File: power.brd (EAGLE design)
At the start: 90 x 77.5 mm, 34 parts, among them IC1 74HC125D, IC2 7805TV, IC3 7815TV

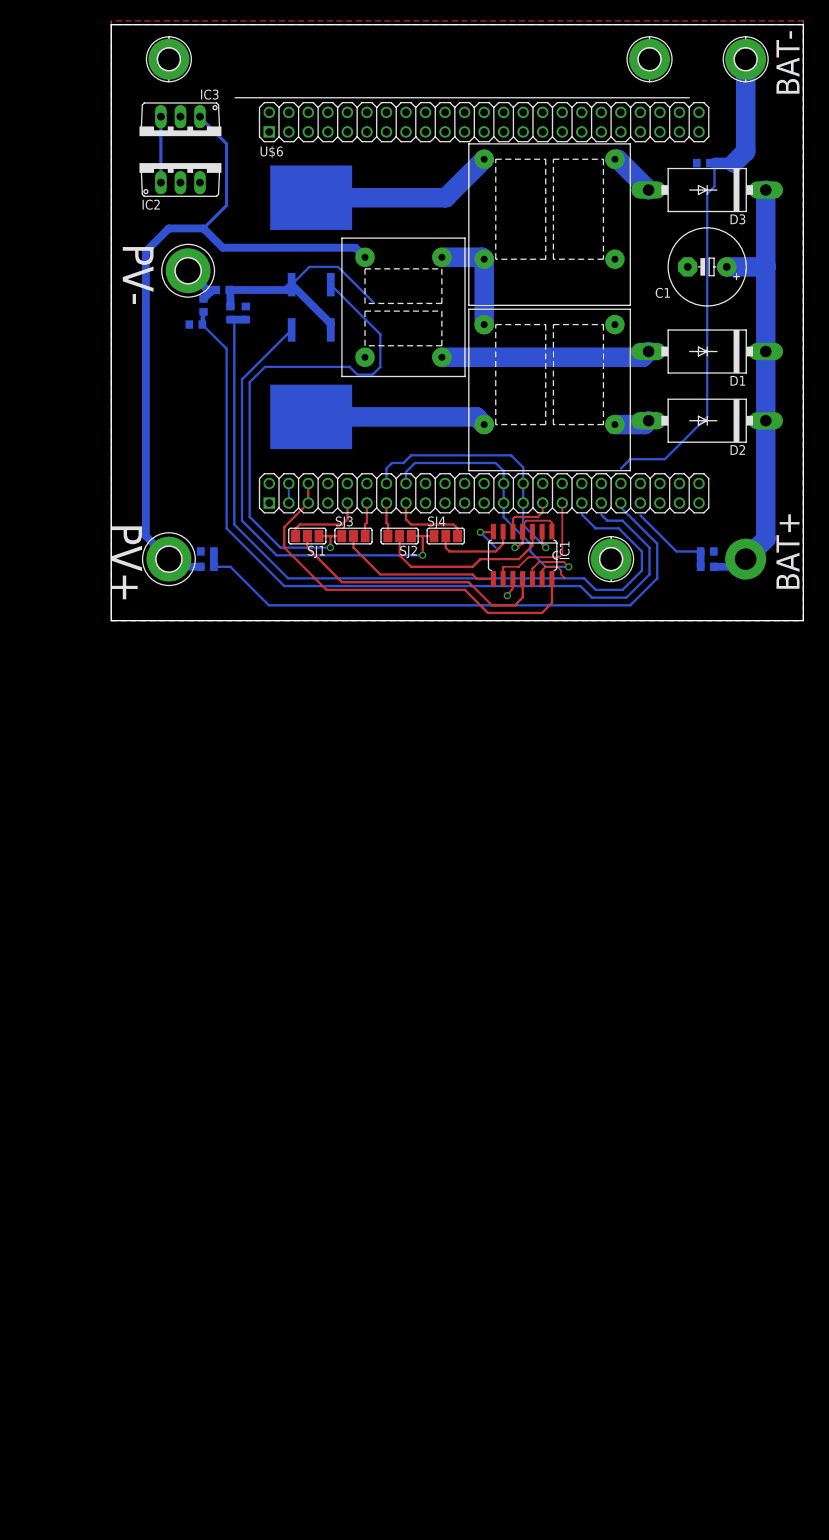
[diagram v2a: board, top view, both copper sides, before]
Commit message: added LTC4151 I2C IV monotors to the schematic and some other fixes.  The prototype doesn't work yet, so watch out.
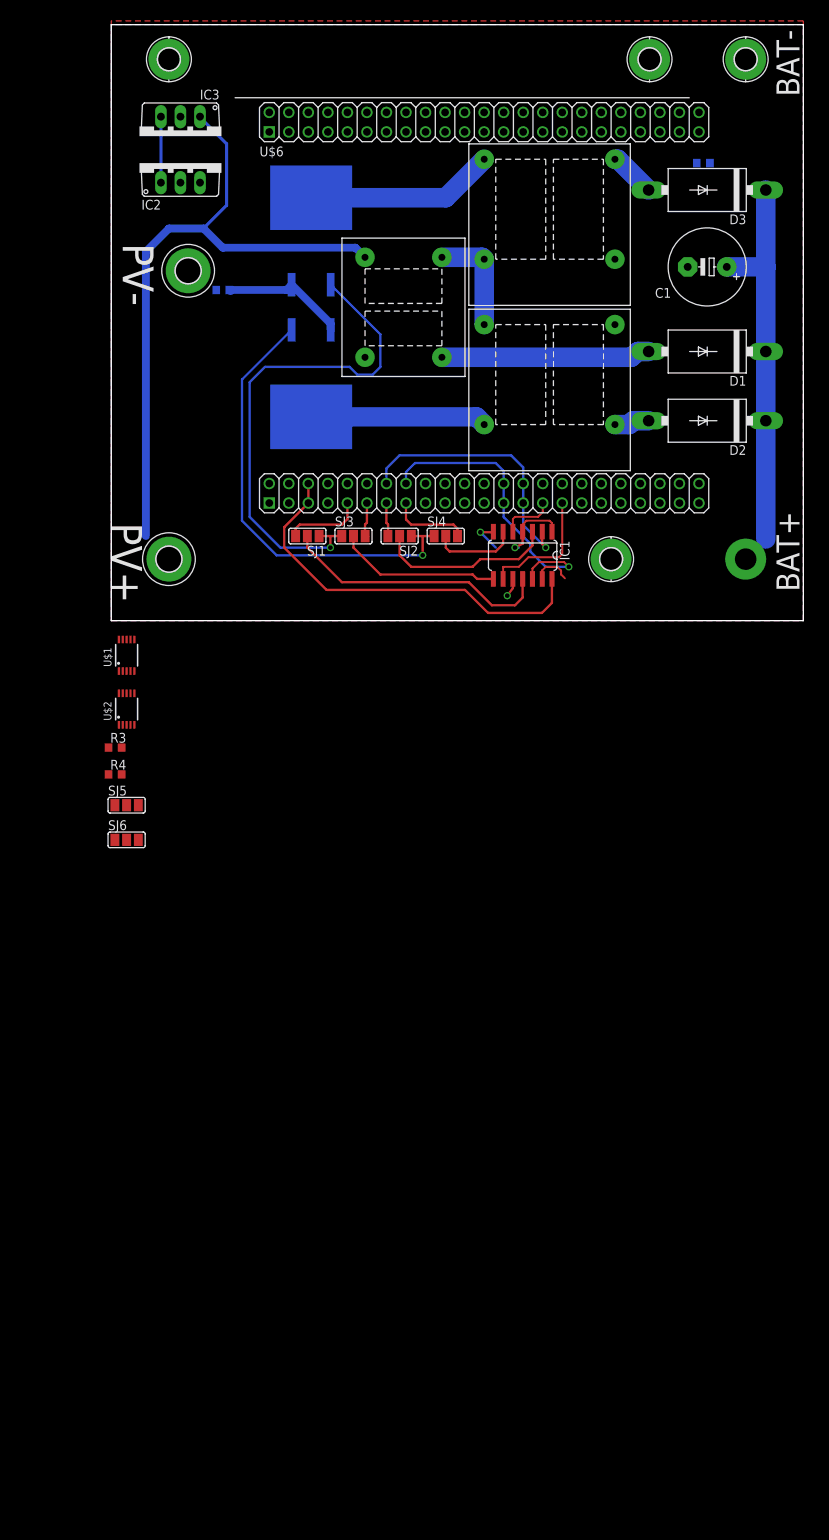
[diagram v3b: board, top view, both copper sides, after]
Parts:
- removed R10, R6, R8: 1k, rcl:R0603
- removed R5, R9: 51k, rcl:R0603
- removed R7: 15k, rcl:R0603
- added SJ5, SJ6: (no value), jumper:SJ_2
- added U$1, U$2: LTC4151, semiconductors:MSOP10
- R3: value 51k -> (none)
- R4: value 1k -> (none)
- moved R4 31.4 mm to (-2.00, -23.0), flipped to the top, turned to 0 degrees
- moved R3 26.4 mm to (-2.00, -19.5), flipped to the top, turned to 0 degrees
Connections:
- removed net N$17: R5.2, R6.2
- removed net N$18: R10.2, R9.2
- removed net VDD_3V3EXP: U$6.49, U$6.50
- new net +3V3: R3.2, R4.2, U$1.8, U$2.8, U$6.49, U$6.50
- new net N$14: R4.1, U$2.6, U$6.63
- new net N$26: SJ6.2, U$2.4
- net GND: now also BAT-.B2,8, SJ5.1, SJ6.1, U$1.9, U$2.3, U$2.9; no longer R1.1, R10.1, R4.1, R6.1, R8.1
- net N$10: now also SJ5.2, U$1.4; no longer R7.2, R8.2
- net N$12: now also C1.+, D1.C, D2.C, D3.C, R1.1, SJ6.3, U$2.1, U$2.2; no longer R3.2, R4.2
- net N$16: now also PV+.B3,3, SJ5.3, U$1.1, U$1.2, U$1.3; no longer PV-.B3,3, R5.1
- net N$4: now also BAT+.B2,8, IC3.1, U$2.10; no longer BAT-.B2,8
- net N$6: now also R2.2, U$1.10; no longer IC3.1, PV+.B3,3, R3.1
- net N$7: now also R3.1, U$2.7, U$6.64; no longer BAT+.B2,8, C1.+, D1.C, D2.C, D3.C, R7.1
- net N$8: now also PV-.B3,3; no longer R2.2, R9.1
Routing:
- net N$17: track 101.3 -> 0.00 mm
- net N$18: track 99.5 -> 0.00 mm
- net N$4: track 64.7 -> 0.00 mm
- net N$7: track 58.7 -> 0.00 mm
- net N$12: track 74.4 -> 50.5 mm
- net N$8: track 32.1 -> 16.4 mm
- net N$10: track 11.8 -> 0.00 mm
- net N$6: track 94.3 -> 85.4 mm
- net N$16: track 6.12 -> 1.41 mm
- net VDD_3V3EXP: track 2.54 -> 0.00 mm

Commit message: whomp
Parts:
- removed IC1: 74HC125D, 74xx-eu:SO14
- removed IC3: 7815TV, linear:TO220V
- removed SJ1, SJ2, SJ3, SJ4: (no value), jumper:SJ_2
- added R10, R11, R12, R13, R14, R15, R16, R17, R18, R19, R20, R21, R22, R23, R24, R25, R26, R27, R28, R29, R30, R7, R8, R9: 0, rcl:R0603
- added R5, R6: 10k, rcl:R0603
- U$7, U$8: value 45NO6LG -> SIA446DJ; device semiconductors:D2PAK-3 -> semiconductors:SC70-6L
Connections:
- removed net N$27: IC2.1, IC3.3
- new net N$17: R9.1, U$6.77
- new net N$18: R10.1, U$6.76
- new net N$30: R5.2, R6.1, U$1.5
- new net N$31: R26.1, U$6.43
- new net N$32: R27.1, U$6.42
- new net N$34: R29.1, U$6.40
- new net N$35: R30.1, U$6.39
- new net N$36: U$6.12
- new net N$39: R19.1, U$6.21
- new net N$40: R18.1, U$6.27
- new net N$41: R17.1, U$6.28
- new net N$42: R16.1, U$6.29
- new net N$43: U$6.30
- new net N$44: R10.2, R12.2, R14.2, R16.2, R18.2, R20.2, R22.2, R24.2, R26.2, R28.2, R30.2, R8.2, U$7.3
- new net N$45: R11.2, R13.2, R15.2, R17.2, R19.2, R21.2, R23.2, R25.2, R27.2, R29.2, R7.2, R9.2, U$8.3
- net GND: now also R6.2; no longer IC1.1, IC1.10, IC1.13, IC1.4, IC1.7, IC3.2
- net N$11: now also R15.1; no longer SJ1.1, SJ3.1, U$8.1
- net N$13: now also R21.1; no longer SJ2.1, SJ4.1, U$7.1
- net N$14: now also U$1.6, U$6.70; no longer U$6.63
- net N$19: now also R11.1, U$6.75; no longer SJ1.3, U$6.55
- net N$2: now also U$8.1, U$8.2, U$8.5, U$8.6; no longer U$8.4
- net N$20: now also R7.1, U$6.87; no longer IC1.3, SJ2.2
- net N$21: now also R8.1, U$6.88; no longer SJ3.3, U$6.57
- net N$22: now also R12.1, U$6.74; no longer SJ4.3, U$6.61
- net N$23: now also R13.1; no longer IC1.2, U$6.60, U$6.74
- net N$24: now also R14.1, U$6.71; no longer IC1.6, SJ4.2
- net N$25: now also R23.1, U$6.46; no longer IC1.11, SJ1.2
- net N$28: now also R24.1, U$6.45; no longer IC1.12, U$6.62, U$6.71, U$6.72
- net N$29: now also R25.1, U$6.44; no longer IC1.8, SJ3.2
- net N$3: now also U$7.1, U$7.2, U$7.5, U$7.6; no longer U$7.4
- net N$33: now also R28.1, U$6.41; no longer SJ2.3, U$6.59
- net N$37: now also R22.1, U$6.11; no longer IC1.5, U$6.75
- net N$38: now also R20.1, U$6.20; no longer IC1.9, U$6.77
- net N$4: now also IC2.1; no longer IC3.1
- net N$7: now also U$1.7, U$6.72; no longer U$6.64
- net N$8: now also R5.1, U$7.4, U$7.7, U$8.4, U$8.7; no longer U$7.3, U$8.3
- net VCC: no longer IC1.14
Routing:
- net N$11: track 66.1 -> 0.00 mm, vias 1 -> 0
- net N$13: track 58.3 -> 0.00 mm, vias 1 -> 0
- net N$28: track 39.5 -> 0.00 mm, vias 1 -> 0
- net N$25: track 35.4 -> 0.00 mm
- net N$23: track 35.0 -> 0.00 mm, vias 1 -> 0
- net N$8: track 16.4 -> 51.4 mm
- net N$20: track 23.3 -> 0.00 mm
- net GND: track 21.5 -> 0.00 mm, vias 3 -> 0
- net N$29: track 21.4 -> 0.00 mm
- net N$38: track 16.6 -> 0.00 mm
- net N$24: track 11.2 -> 0.00 mm
- net N$19: track 10.3 -> 0.00 mm
- net N$22: track 10.3 -> 0.00 mm
- net N$27: track 8.58 -> 0.00 mm
- net N$37: track 7.09 -> 0.00 mm
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
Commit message: don't worry, it's not as bad as it looks
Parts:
- R3, R4: value (none) -> 47k
- moved R29 198.5 mm to (67.3, 66.0), flipped to the bottom
- moved R30 196.0 mm to (64.8, 66.0), flipped to the bottom, turned to 90 degrees
- moved R27 195.2 mm to (71.1, 66.0), flipped to the bottom, turned to 90 degrees
- moved R28 193.0 mm to (69.8, 66.0), flipped to the bottom, turned to 90 degrees
- moved R25 191.1 mm to (72.4, 66.0), flipped to the bottom, turned to 90 degrees
- moved R26 189.7 mm to (73.7, 66.0), flipped to the bottom, turned to 90 degrees
- moved R23 187.5 mm to (74.9, 66.0), flipped to the bottom, turned to 90 degrees
- moved R24 186.0 mm to (76.2, 66.0), flipped to the bottom, turned to 90 degrees
- moved R21 169.4 mm to (31.8, 66.0), flipped to the bottom, turned to 90 degrees
- moved R22 168.3 mm to (30.5, 66.0), flipped to the bottom, turned to 90 degrees
- moved R19 167.3 mm to (43.2, 66.0), flipped to the bottom, turned to 90 degrees
- moved R20 165.7 mm to (41.9, 66.0), flipped to the bottom, turned to 90 degrees
- moved R17 165.1 mm to (52.1, 66.0), flipped to the bottom, turned to 90 degrees
- moved R18 163.2 mm to (50.8, 66.0), flipped to the bottom, turned to 90 degrees
- moved R15 161.3 mm to (54.6, 66.0), flipped to the bottom, turned to 90 degrees
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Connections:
- removed net N$36: U$6.12
- removed net N$43: U$6.30
- net N$11: now also U$6.30
- net N$13: now also U$6.12
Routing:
- net N$6: track 85.4 -> 0.00 mm
- net N$8: track 51.4 -> 0.00 mm
- net N$12: track 50.5 -> 0.00 mm
- net VCC: track 46.0 -> 0.00 mm
- net N$15: track 27.2 -> 0.00 mm
- net N$2: track 23.9 -> 0.00 mm
- net N$3: track 23.6 -> 0.00 mm
- net N$1: track 14.1 -> 0.00 mm
- net N$5: track 6.04 -> 0.00 mm
- net N$9: track 4.59 -> 0.00 mm
- net N$16: track 1.41 -> 0.00 mm

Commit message: still working on it
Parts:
- added C2: 100pf, rcl:C0603K
- R5, R6: value 10k -> 12k
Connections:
- net GND: now also C2.1
- net N$30: now also C2.2
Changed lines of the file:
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@@
 <element name="SJ5" library="jumper" package="SJ_2" value="" x="15.24" y="2.54" rot="MR180"/>
 <element name="SJ6" library="jumper" package="SJ_2" value="" x="80.01" y="11.43" rot="MR180"/>
-<element name="R5" library="rcl" package="R0603" value="10k" x="28.8" y="7.22" rot="MR0"/>
-<element name="R6" library="rcl" package="R0603" value="10k" x="21.815" y="4.76" rot="MR0"/>
+<element name="R5" library="rcl" package="R0603" value="12k" x="28.8" y="7.22" rot="MR0"/>
+<element name="R6" library="rcl" package="R0603" value="12k" x="21.815" y="4.76" rot="MR0"/>
 <element name="R7" library="rcl" package="R0603" value="0" x="68.58" y="7.62" rot="MR270"/>
 <element name="R8" library="rcl" package="R0603" value="0" x="71.12" y="7.62" rot="MR270"/>
@@
 <element name="R29" library="rcl" package="R0603" value="0" x="67.31" y="66.04" rot="MR0"/>
 <element name="R30" library="rcl" package="R0603" value="0" x="64.77" y="66.04" rot="MR90"/>
+<element name="C2" library="rcl" package="C0603K" value="100pf" x="-1.27" y="-6.35"/>
 </elements>
 <signals>
@@
 <contactref element="SJ6" pad="1"/>
 <contactref element="R6" pad="2"/>
+<contactref element="C2" pad="1"/>
 <wire x1="77.96" y1="15.74" x2="82.06" y2="15.24" width="0" layer="19" extent="16-16"/>
 <wire x1="74.93" y1="14.605" x2="77.96" y2="15.74" width="0" layer="19" extent="16-16"/>
 <wire x1="78.486" y1="11.43" x2="74.93" y2="12.065" width="0" layer="19" extent="16-16"/>
-<wire x1="13.19" y1="6.85" x2="19.05" y2="12.065" width="0" layer="19" extent="16-16"/>
-<wire x1="13.716" y1="2.54" x2="13.19" y2="6.85" width="0" layer="19" extent="16-16"/>
-<wire x1="20.965" y1="4.76" x2="7.78" y2="30.48" width="0" layer="19" extent="16-16"/>
+<wire x1="20.965" y1="4.76" x2="19.05" y2="12.065" width="0" layer="19" extent="16-16"/>
+<wire x1="13.716" y1="2.54" x2="20.965" y2="4.76" width="0" layer="19" extent="16-16"/>
+<wire x1="13.19" y1="6.85" x2="13.716" y2="2.54" width="0" layer="19" extent="16-16"/>
+<wire x1="-2.145" y1="-6.35" x2="13.716" y2="2.54" width="0" layer="19" extent="1-16"/>
+<wire x1="40.64" y1="44.45" x2="62.23" y2="31.45" width="0" layer="19" extent="1-1"/>
 </signal>
 <signal name="SYS_5V">
@@
 <contactref element="R6" pad="1"/>
 <contactref element="R5" pad="2"/>
+<contactref element="C2" pad="2"/>
 <wire x1="22.665" y1="4.76" x2="27.95" y2="7.22" width="0" layer="19" extent="16-16"/>
 <wire x1="17.29" y1="5.35" x2="22.665" y2="4.76" width="0" layer="19" extent="16-16"/>
+<wire x1="-0.395" y1="-6.35" x2="17.29" y2="5.35" width="0" layer="19" extent="1-16"/>
 </signal>
 <signal name="N$17">

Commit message: almost there
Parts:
- moved C2 25.0 mm to (21.6, 3.81), flipped to the bottom
- moved R4 17.5 mm to (73.5, 7.21), turned to 270 degrees
- moved R3 17.1 mm to (73.8, 3.40), turned to 270 degrees
- moved R8 11.5 mm to (69.8, 19.1), turned to 90 degrees
- moved R10 11.5 mm to (54.6, 19.1), turned to 90 degrees
- moved R12 11.5 mm to (52.1, 19.1), turned to 90 degrees
- moved R14 11.4 mm to (49.5, 19.1), turned to 90 degrees
- moved R20 10.5 mm to (44.5, 55.9), turned to 270 degrees
- moved R30 10.5 mm to (67.3, 55.9), turned to 270 degrees
- moved R16 10.2 mm to (54.6, 55.9), turned to 270 degrees
- moved R18 10.2 mm to (52.1, 55.9), turned to 270 degrees
- moved R22 10.2 mm to (31.8, 55.9), turned to 270 degrees
- moved R24 10.2 mm to (74.9, 55.9), turned to 270 degrees
- moved R26 10.2 mm to (72.4, 55.9), turned to 270 degrees
- moved R28 10.2 mm to (69.8, 55.9), turned to 270 degrees
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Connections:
- removed net N$39: R19.1, U$6.21
- new net N$36: R19.1, U$6.20
- net N$38: now also U$6.21; no longer U$6.20

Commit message: need a snapshot here
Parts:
- moved U$8 33.7 mm to (12.7, 39.4), turned to 0 degrees
- moved D3 17.5 mm to (76.2, 35.6)
- moved U$7 16.3 mm to (12.7, 35.6), turned to 0 degrees
- moved D1 3.04 mm to (76.2, 29.2)
- moved C1 2.97 mm to (76.2, 45.7)
- moved D2 1.21 mm to (76.2, 22.9)
- moved IC2 0.67 mm to (6.35, 57.1)
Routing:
- removed copper zone on layer 16, net GND
